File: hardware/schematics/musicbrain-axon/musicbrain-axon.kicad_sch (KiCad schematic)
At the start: 52 parts, among them J1 BUSBOARD (J25+J19), J2 USBC16, J3 MAGJACK (paneel), J4 DEBUG, SW1 SW_TACT, SW2 SW_TACT, U1 ESP32-S3-WROOM-1U, U2 W5500, U3 AMS1117-33, Y1 XTAL4

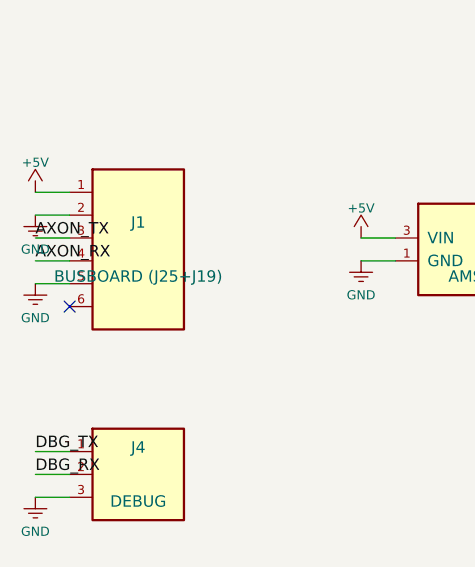
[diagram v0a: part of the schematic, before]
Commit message: Axon J1: alle 6 pinnen, 2+4 gegroepeerd (5V/GND->J25, GND/RX/TX/GND->J19)
RX op pin 4, TX op pin 5: beide kabels recht 1:1 (UART-kruising in de
pinvolgorde). Per-pin silk-labels uitgelijnd onder de pads (0.8mm-font,
silk-helper met optionele grootte). Geroute DRC 0/0; kabeltabel in README.

Co-Authored-By: Claude Fable 5 <noreply@anthropic.com>
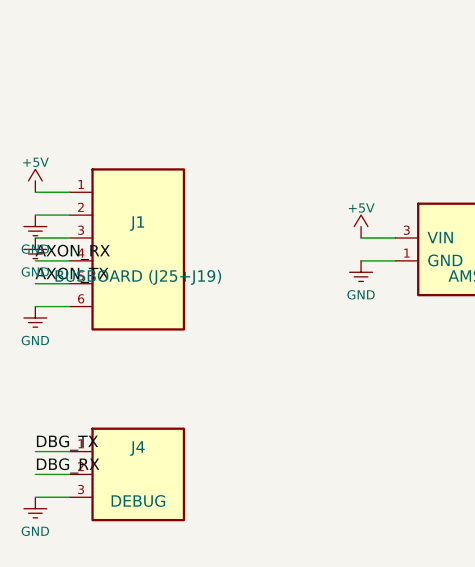
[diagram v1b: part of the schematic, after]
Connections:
- net AXON_TX: now also J1.5 (Pin_5); no longer J1.3 (Pin_3)
- net GND: now also J1.3 (Pin_3), J1.6 (Pin_6); no longer J1.5 (Pin_5)
- no-connect marks 41 -> 40
